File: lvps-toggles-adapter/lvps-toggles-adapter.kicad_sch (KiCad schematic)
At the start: 19 parts, among them J1 Toggle 1 in, J10 Toggle 2 out, J11 Toggle 3 out, J12 Toggle 4 out, J13 Bias/heat out, J14 bridgeports out, J15 Other heat connection, J2 Toggle 2 in, J3 Toggle 3 in, J4 Toggle 4 in, J5 Bias in, J6 Heater, J7 BCS-110-L-D-TE, J8 Toggle 1 out, J9 Sense passthrough

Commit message: toggles adapter: cleanup
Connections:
- net GND: now also J11.5 (Pin_5), J11.6 (Pin_6), J11.7 (Pin_7), J12.5 (Pin_5), J12.6 (Pin_6), J12.7 (Pin_7), J8.5 (Pin_5), J8.6 (Pin_6), J8.7 (Pin_7)

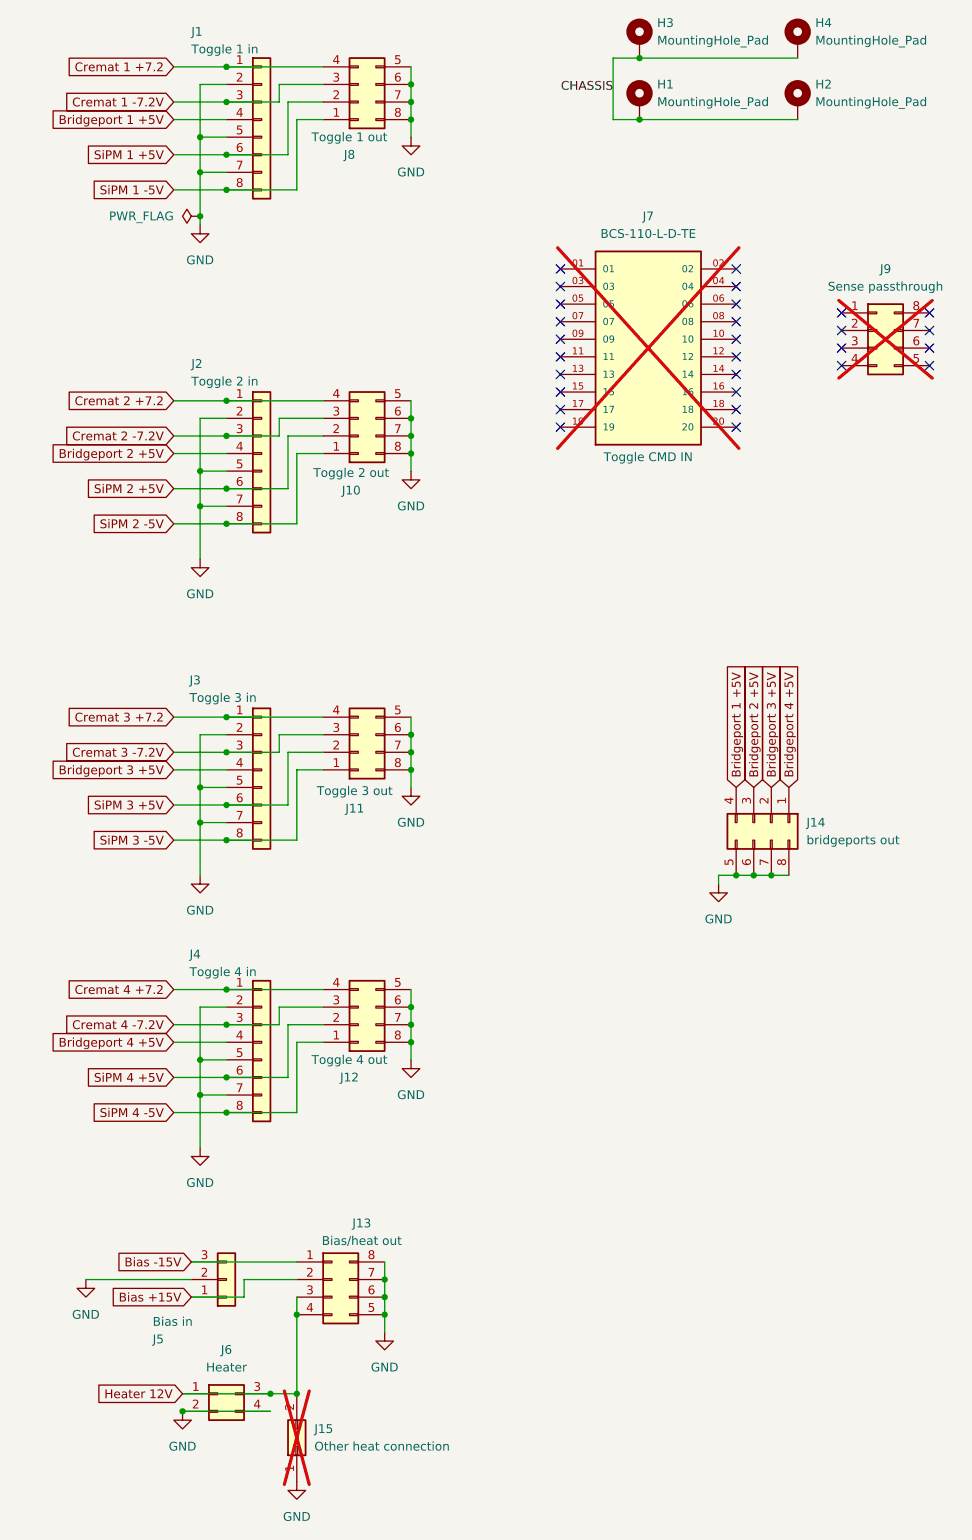
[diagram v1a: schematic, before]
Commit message: junction board updates
. add daqbox lines
. fix heater routing
. remove unused toggle lines
. swap to nicer/cheaper/smaller 4-pin Molex for bias/preamp
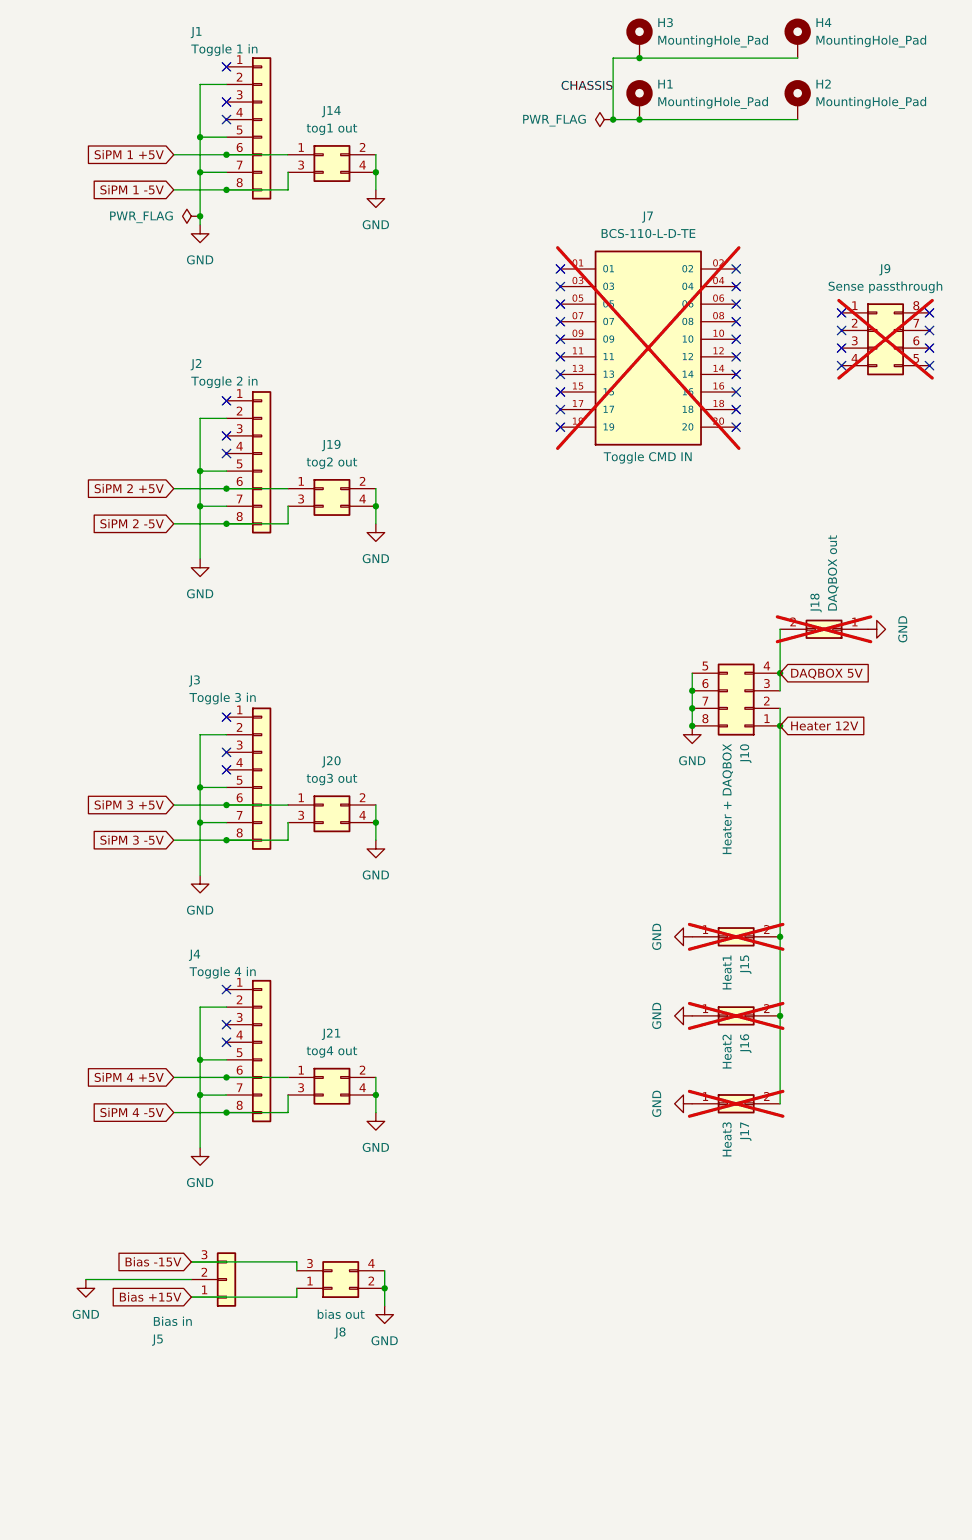
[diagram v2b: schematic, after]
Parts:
- removed J11: Toggle 3 out, Library:HARWIN_M80-5L10842MC, symbol Connector_Generic:Conn_02x04_Counter_Clockwise
- removed J12: Toggle 4 out, Library:HARWIN_M80-5L10842MC, symbol Connector_Generic:Conn_02x04_Counter_Clockwise
- removed J13: Bias/heat out, Library:HARWIN_M80-5L10842MC, symbol Connector_Generic:Conn_02x04_Counter_Clockwise
- removed J14: bridgeports out, Library:HARWIN_M80-5L10842MC, symbol Connector_Generic:Conn_02x04_Counter_Clockwise
- removed J6: Heater, Connector_PinHeader_2.54mm:PinHeader_2x02_P2.54mm_Vertical, symbol Connector_Generic:Conn_02x02_Top_Bottom
- removed J8: Toggle 1 out, Library:HARWIN_M80-5L10842MC, symbol Connector_Generic:Conn_02x04_Counter_Clockwise
- added J14: tog1 out, Library:MOLEX_5031750400, symbol Connector_Generic:Conn_02x02_Odd_Even
- added J16: Heat2, Connector_PinHeader_2.54mm:PinHeader_2x01_P2.54mm_Vertical, symbol Connector_Generic:Conn_02x01
- added J17: Heat3, Connector_PinHeader_2.54mm:PinHeader_2x01_P2.54mm_Vertical, symbol Connector_Generic:Conn_02x01
- added J18: DAQBOX out, Connector_PinHeader_2.54mm:PinHeader_2x01_P2.54mm_Vertical, symbol Connector_Generic:Conn_02x01
- added J19: tog2 out, Library:MOLEX_5031750400, symbol Connector_Generic:Conn_02x02_Odd_Even
- added J20: tog3 out, Library:MOLEX_5031750400, symbol Connector_Generic:Conn_02x02_Odd_Even
- added J21: tog4 out, Library:MOLEX_5031750400, symbol Connector_Generic:Conn_02x02_Odd_Even
- added J8: bias out, Library:MOLEX_5031750400, symbol Connector_Generic:Conn_02x02_Odd_Even
- J10: value Toggle 2 out -> Heater + DAQBOX; footprint Library:HARWIN_M80-5L10842MC -> Connector_PinSocket_2.54mm:PinSocket_2x04_P2.54mm_Vertical
- J15: value Other heat connection -> Heat1
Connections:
- net Bias +15V: now also J8.1 (Pin_1)
- net Bias -15V: now also J8.3 (Pin_3)
- net GND: now also J14.2 (Pin_2), J14.4 (Pin_4), J16.1 (Pin_1), J17.1 (Pin_1), J18.1 (Pin_1), J19.2 (Pin_2), J19.4 (Pin_4), J20.2 (Pin_2), J20.4 (Pin_4), J21.2 (Pin_2), J21.4 (Pin_4), J8.2 (Pin_2), J8.4 (Pin_4)
- net Heater 12V: now also J10.1 (Pin_1), J10.2 (Pin_2), J16.2 (Pin_2), J17.2 (Pin_2)
- net SiPM 1 +5V: now also J14.1 (Pin_1)
- net SiPM 1 -5V: now also J14.3 (Pin_3)
- net SiPM 2 +5V: now also J19.1 (Pin_1); no longer J10.2 (Pin_2)
- net SiPM 2 -5V: now also J19.3 (Pin_3); no longer J10.1 (Pin_1)
- net SiPM 3 +5V: now also J20.1 (Pin_1)
- net SiPM 3 -5V: now also J20.3 (Pin_3)
- net SiPM 4 +5V: now also J21.1 (Pin_1)
- net SiPM 4 -5V: now also J21.3 (Pin_3)
- net Bridgeport 1 +5V: no longer names the net of J1.4 (Pin_4)
- net Bridgeport 2 +5V: no longer names the net of J2.4 (Pin_4)
- net Bridgeport 3 +5V: no longer names the net of J3.4 (Pin_4)
- net Bridgeport 4 +5V: no longer names the net of J4.4 (Pin_4)
- net Cremat 1 +7.2: no longer names the net of J1.1 (Pin_1)
- net Cremat 1 -7.2V: no longer names the net of J1.3 (Pin_3)
- net Cremat 2 +7.2: no longer names the net of J2.1 (Pin_1)
- net Cremat 2 +7.2: no longer J10.4 (Pin_4)
- net Cremat 2 -7.2V: no longer names the net of J2.3 (Pin_3)
- net Cremat 2 -7.2V: no longer J10.3 (Pin_3)
- net Cremat 3 +7.2: no longer names the net of J3.1 (Pin_1)
- net Cremat 3 -7.2V: no longer names the net of J3.3 (Pin_3)
- net Cremat 4 +7.2: no longer names the net of J4.1 (Pin_1)
- net Cremat 4 -7.2V: no longer names the net of J4.3 (Pin_3)
- new net DAQBOX 5V: J10.3 (Pin_3), J10.4 (Pin_4), J18.2 (Pin_2)
- no-connect marks 28 -> 40
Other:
- moved on the sheet: J15
